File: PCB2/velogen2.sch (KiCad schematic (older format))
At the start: 34 parts, among them J1 DYN, J2 Conn_01x05_Male, J3 AUX0, J4 AUX1, J5 AUX2, J6 BAT, Q1 BSS123, Q2 DMP10H400SE, SW1 SW_SPST, U1 DCDC_mod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

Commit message: Added Schottkey diode; Clean up ERC
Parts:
- added D6, D7: B5819WS, Diode_SMD:D_SOD-323, symbol Device:D_Schottky
- C1, C2, C3, C4: symbol Device:C -> velogen2-rescue:C-Device
- D1, D2, D3, D4: symbol Device:D_Schottky -> velogen2-rescue:D_Schottky-Device
- D5: symbol Device:D_Zener -> velogen2-rescue:D_Zener-Device
- J1, J6: symbol Connector:Conn_01x02_Male -> velogen2-rescue:Conn_01x02_Male-Connector
- J2: symbol Connector:Conn_01x05_Male -> velogen2-rescue:Conn_01x05_Male-Connector
- J3, J4, J5: symbol Connector:Conn_01x03_Male -> velogen2-rescue:Conn_01x03_Male-Connector
- Q1: symbol Transistor_FET:BSS123 -> velogen2-rescue:BSS123-Transistor_FET
- Q2: symbol Device:Q_PMOS_GDS -> velogen2-rescue:Q_PMOS_GDS-Device
- R1, R2, R3, R4, R5, R6, R7: symbol Device:R -> velogen2-rescue:R-Device
- SW1: symbol Switch:SW_SPST -> velogen2-rescue:SW_SPST-Switch
- TP1, TP2, TP3, TP4: symbol Connector:TestPoint -> velogen2-rescue:TestPoint-Connector
- U1: symbol myStuff:DCDC_mod -> velogen2-rescue:DCDC_mod-myStuff
- U2: symbol RF_Module:ESP32-WROOM-32 -> velogen2-rescue:ESP32-WROOM-32-RF_Module
- U3: symbol Analog_ADC:INA219BxD -> velogen2-rescue:INA219BxD-Analog_ADC
- U4: symbol myStuff:DISP_I2C_EBAY -> velogen2-rescue:DISP_I2C_EBAY-myStuff
- U5: symbol myStuff:POGO_PROG -> velogen2-rescue:POGO_PROG-myStuff
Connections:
- net +3V3: now also D6.1 (K)
- net GND: now also D7.2 (A)
- net speedPulse: now also D6.2 (A), D7.1 (K)
- no-connect marks 0 -> 13

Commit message: clean up schematic symbols
  * re-associate standard symbols with the standard library (needs to be
    installed)
  * remove `myStuff` library. Symbols from there are now in rescue.lib
  * make the 3V3 enable switch a jumper poking out trough the case
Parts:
- removed Q1: BSS123, Package_TO_SOT_SMD:SOT-23, symbol velogen2-rescue:BSS123-Transistor_FET
- added Q1: BSS138, Package_TO_SOT_SMD:SOT-23, symbol Transistor_FET:BSS138
- C1, C2, C3, C4: symbol velogen2-rescue:C-Device -> Device:C
- D1, D2, D3, D4: symbol velogen2-rescue:D_Schottky-Device -> Device:D_Schottky
- D5: symbol velogen2-rescue:D_Zener-Device -> Device:D_Zener
- J1, J6: symbol velogen2-rescue:Conn_01x02_Male-Connector -> Connector:Conn_01x02_Male
- J2: symbol velogen2-rescue:Conn_01x05_Male-Connector -> Connector:Conn_01x05_Male
- J3, J4, J5: symbol velogen2-rescue:Conn_01x03_Male-Connector -> Connector:Conn_01x03_Male
- Q2: symbol velogen2-rescue:Q_PMOS_GDS-Device -> Device:Q_PMOS_GDS
- R1, R2, R3, R4, R5, R6, R7: symbol velogen2-rescue:R-Device -> Device:R
- SW1: footprint Connector_JST:JST_EH_B2B-EH-A_1x02_P2.50mm_Vertical -> Connector_PinHeader_2.54mm:PinHeader_1x02_P2.54mm_Horizontal; symbol velogen2-rescue:SW_SPST-Switch -> Switch:SW_SPST
- TP1, TP2, TP3, TP4: symbol velogen2-rescue:TestPoint-Connector -> Connector:TestPoint
- U2: symbol velogen2-rescue:ESP32-WROOM-32-RF_Module -> RF_Module:ESP32-WROOM-32
- U3: symbol velogen2-rescue:INA219BxD-Analog_ADC -> Analog_ADC:INA219BxD

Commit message: sch: fix some component names
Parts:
- removed Q1: BSS138, Package_TO_SOT_SMD:SOT-23, symbol Transistor_FET:BSS138
- added Q1: BSS123, Package_TO_SOT_SMD:SOT-23, symbol Transistor_FET:BSS123
- D1, D2, D3, D4: value SS32 -> SS310
- SW1: value SW_SPST -> JMP
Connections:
- wire segments 87 -> 88
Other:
- moved on the sheet: D6, D7
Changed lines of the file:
@@
 encoding utf-8
 Sheet 1 1
-Title ""
-Date ""
-Rev ""
+Title "Velogen"
+Date "2020-09-22"
+Rev "-"
 Comp ""
 Comment1 ""
@@
 P 1550 1400
 F 0 "D1" V 1504 1480 50  0000 L CNN
-F 1 "SS32" V 1595 1480 50  0000 L CNN
+F 1 "SS310" V 1595 1480 50  0000 L CNN
 F 2 "Diode_SMD:D_SMC" H 1550 1400 50  0001 C CNN
 F 3 "~" H 1550 1400 50  0001 C CNN
@@
 P 2300 1400
 F 0 "D3" V 2254 1480 50  0000 L CNN
-F 1 "SS32" V 2345 1480 50  0000 L CNN
+F 1 "SS310" V 2345 1480 50  0000 L CNN
 F 2 "Diode_SMD:D_SMC" H 2300 1400 50  0001 C CNN
 F 3 "~" H 2300 1400 50  0001 C CNN
@@
 P 1550 1800
 F 0 "D2" V 1504 1880 50  0000 L CNN
-F 1 "SS32" V 1595 1880 50  0000 L CNN
+F 1 "SS310" V 1595 1880 50  0000 L CNN
 F 2 "Diode_SMD:D_SMC" H 1550 1800 50  0001 C CNN
 F 3 "~" H 1550 1800 50  0001 C CNN
@@
 P 2300 1800
 F 0 "D4" V 2254 1880 50  0000 L CNN
-F 1 "SS32" V 2345 1880 50  0000 L CNN
+F 1 "SS310" V 2345 1880 50  0000 L CNN
 F 2 "Diode_SMD:D_SMC" H 2300 1800 50  0001 C CNN
 F 3 "~" H 2300 1800 50  0001 C CNN
@@
 P 1550 5150
 F 0 "SW1" V 1504 5248 50  0000 L CNN
-F 1 "SW_SPST" V 1595 5248 50  0000 L CNN
+F 1 "JMP" V 1595 5248 50  0000 L CNN
 F 2 "Connector_PinHeader_2.54mm:PinHeader_1x02_P2.54mm_Horizontal" H 1550 5150 50  0001 C CNN
 F 3 "~" H 1550 5150 50  0001 C CNN
@@
 Wire Wire Line
 	2750 1750 2750 1600
-Text Label 2750 2550 1    50   ~ 0
+Text Label 3200 3000 2    50   ~ 0
 speedPulse
 Text Label 6750 3750 2    50   ~ 0
@@
 L Device:D_Schottky D6
 U 1 1 5F65588B
-P 2850 3050
-F 0 "D6" H 2850 3267 50  0000 C CNN
-F 1 "B5819WS" H 2850 3176 50  0000 C CNN
-F 2 "Diode_SMD:D_SOD-323" H 2850 3050 50  0001 C CNN
-F 3 "https://www.mccsemi.com/pdf/Products/B5817WS-B5819WS(SOD-323).PDF" H 2850 3050 50  0001 C CNN
-	1    2850 3050
+P 2450 2800
+F 0 "D6" H 2450 3017 50  0000 C CNN
+F 1 "B5819WS" H 2450 2926 50  0000 C CNN
+F 2 "Diode_SMD:D_SOD-323" H 2450 2800 50  0001 C CNN
+F 3 "https://www.mccsemi.com/pdf/Products/B5817WS-B5819WS(SOD-323).PDF" H 2450 2800 50  0001 C CNN
+	1    2450 2800
 	0    1    1    0
 $EndComp
@@
 L Device:D_Schottky D7
 U 1 1 5F657E57
-P 2850 3650
-F 0 "D7" H 2850 3867 50  0000 C CNN
-F 1 "B5819WS" H 2850 3776 50  0000 C CNN
-F 2 "Diode_SMD:D_SOD-323" H 2850 3650 50  0001 C CNN
-F 3 "https://www.mccsemi.com/pdf/Products/B5817WS-B5819WS(SOD-323).PDF" H 2850 3650 50  0001 C CNN
-	1    2850 3650
-	0    1    1    0
-$EndComp
-Wire Wire Line
-	2850 3200 2850 3350
-Wire Wire Line
-	2850 3350 2750 3350
-Connection ~ 2850 3350
-Wire Wire Line
-	2850 3350 2850 3500
-Wire Wire Line
-	2750 2050 2750 3350
+P 2450 3200
+F 0 "D7" H 2450 3417 50  0000 C CNN
+F 1 "B5819WS" H 2450 3326 50  0000 C CNN
+F 2 "Diode_SMD:D_SOD-323" H 2450 3200 50  0001 C CNN
+F 3 "https://www.mccsemi.com/pdf/Products/B5817WS-B5819WS(SOD-323).PDF" H 2450 3200 50  0001 C CNN
+	1    2450 3200
+	0    1    1    0
+$EndComp
+Wire Wire Line
+	2450 2950 2450 3000
+Connection ~ 2450 3000
+Wire Wire Line
+	2450 3000 2450 3050
+Wire Wire Line
+	2750 2050 2750 3000
 $Comp
 L power:+3V3 #PWR04
 U 1 1 5F688C96
-P 2850 2900
-F 0 "#PWR04" H 2850 2750 50  0001 C CNN
-F 1 "+3V3" H 2865 3073 50  0000 C CNN
-F 2 "" H 2850 2900 50  0001 C CNN
-F 3 "" H 2850 2900 50  0001 C CNN
-	1    2850 2900
+P 2450 2650
+F 0 "#PWR04" H 2450 2500 50  0001 C CNN
+F 1 "+3V3" H 2465 2823 50  0000 C CNN
+F 2 "" H 2450 2650 50  0001 C CNN
+F 3 "" H 2450 2650 50  0001 C CNN
+	1    2450 2650
 	1    0    0    -1
 $EndComp
@@
 L power:GND #PWR05
 U 1 1 5F6962B6
-P 2850 3800
-F 0 "#PWR05" H 2850 3550 50  0001 C CNN
-F 1 "GND" H 2855 3627 50  0000 C CNN
-F 2 "" H 2850 3800 50  0001 C CNN
-F 3 "" H 2850 3800 50  0001 C CNN
-	1    2850 3800
+P 2450 3350
+F 0 "#PWR05" H 2450 3100 50  0001 C CNN
+F 1 "GND" H 2455 3177 50  0000 C CNN
+F 2 "" H 2450 3350 50  0001 C CNN
+F 3 "" H 2450 3350 50  0001 C CNN
+	1    2450 3350
 	1    0    0    -1
 $EndComp
@@
 NoConn ~ 5050 5250
 $Comp
-L Transistor_FET:BSS138 Q1
-U 1 1 5F65DFE4
+L Transistor_FET:BSS123 Q1
+U 1 1 5F6AB46B
 P 3350 2200
 F 0 "Q1" H 3555 2246 50  0000 L CNN
-F 1 "BSS138" H 3555 2155 50  0000 L CNN
+F 1 "BSS123" H 3555 2155 50  0000 L CNN
 F 2 "Package_TO_SOT_SMD:SOT-23" H 3550 2125 50  0001 L CIN
-F 3 "https://www.onsemi.com/pub/Collateral/BSS138-D.PDF" H 3350 2200 50  0001 L CNN
+F 3 "http://www.diodes.com/assets/Datasheets/ds30366.pdf" H 3350 2200 50  0001 L CNN
 	1    3350 2200
 	-1   0    0    -1
 $EndComp
+Wire Wire Line
+	2450 3000 2750 3000
+Connection ~ 2750 3000
+Wire Wire Line
+	2750 3000 3200 3000
 $EndSCHEMATC

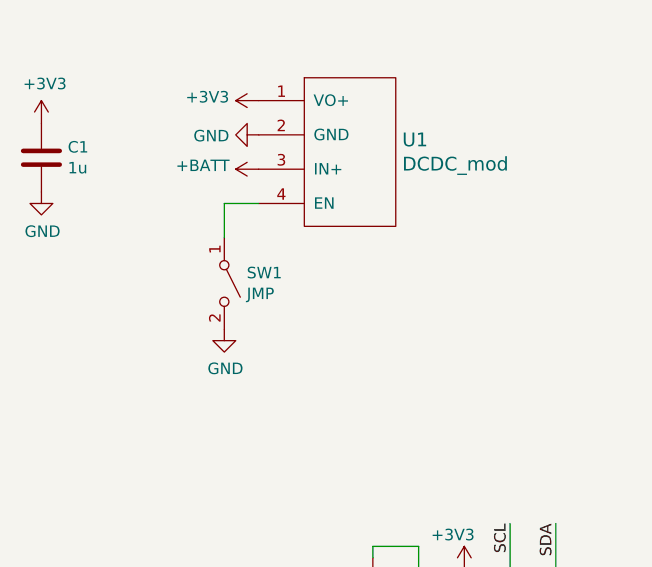
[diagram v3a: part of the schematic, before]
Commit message: put propper package (SMA) for diodes
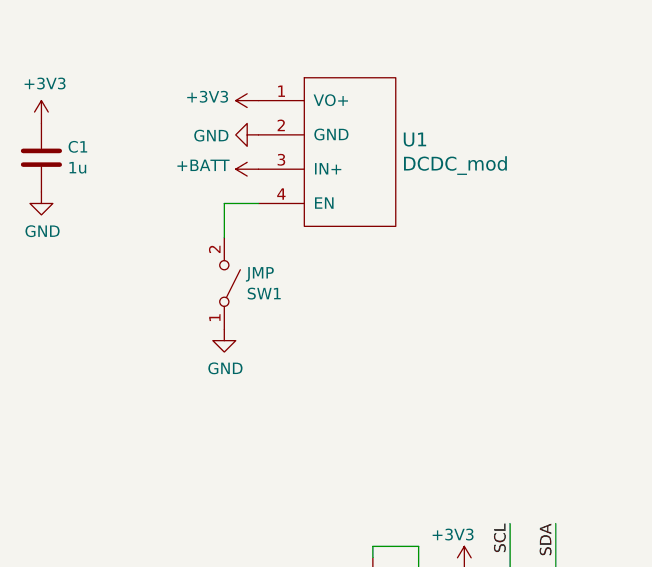
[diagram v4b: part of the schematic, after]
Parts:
- D1, D2, D3, D4: footprint Diode_SMD:D_SMC -> Diode_SMD:D_SMA
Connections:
- net GND: now also SW1.1 (A); no longer SW1.2 (B)
- net at U1.4 (EN): now also SW1.2 (B); no longer SW1.1 (A)
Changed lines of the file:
@@
 F 0 "D1" V 1504 1480 50  0000 L CNN
 F 1 "SS310" V 1595 1480 50  0000 L CNN
-F 2 "Diode_SMD:D_SMC" H 1550 1400 50  0001 C CNN
+F 2 "Diode_SMD:D_SMA" H 1550 1400 50  0001 C CNN
 F 3 "~" H 1550 1400 50  0001 C CNN
 	1    1550 1400
@@
 F 0 "D3" V 2254 1480 50  0000 L CNN
 F 1 "SS310" V 2345 1480 50  0000 L CNN
-F 2 "Diode_SMD:D_SMC" H 2300 1400 50  0001 C CNN
+F 2 "Diode_SMD:D_SMA" H 2300 1400 50  0001 C CNN
 F 3 "~" H 2300 1400 50  0001 C CNN
 	1    2300 1400
@@
 F 0 "D2" V 1504 1880 50  0000 L CNN
 F 1 "SS310" V 1595 1880 50  0000 L CNN
-F 2 "Diode_SMD:D_SMC" H 1550 1800 50  0001 C CNN
+F 2 "Diode_SMD:D_SMA" H 1550 1800 50  0001 C CNN
 F 3 "~" H 1550 1800 50  0001 C CNN
 	1    1550 1800
@@
 F 0 "D4" V 2254 1880 50  0000 L CNN
 F 1 "SS310" V 2345 1880 50  0000 L CNN
-F 2 "Diode_SMD:D_SMC" H 2300 1800 50  0001 C CNN
+F 2 "Diode_SMD:D_SMA" H 2300 1800 50  0001 C CNN
 F 3 "~" H 2300 1800 50  0001 C CNN
 	1    2300 1800
@@
 F 3 "~" H 1550 5150 50  0001 C CNN
 	1    1550 5150
-	0    1    1    0
-$EndComp
-Wire Wire Line
+	0    1    -1   0
+$EndComp
+Wire Wire Line

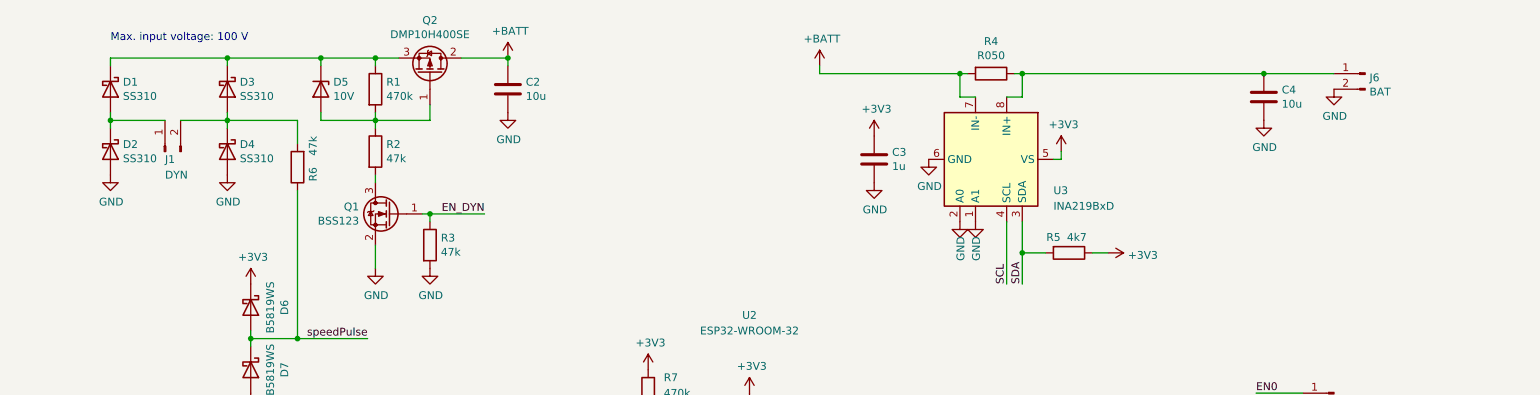
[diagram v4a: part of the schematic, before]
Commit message: did some routing of the power rails
  * kinda stuck on the 3V3, might need to re-consider placement
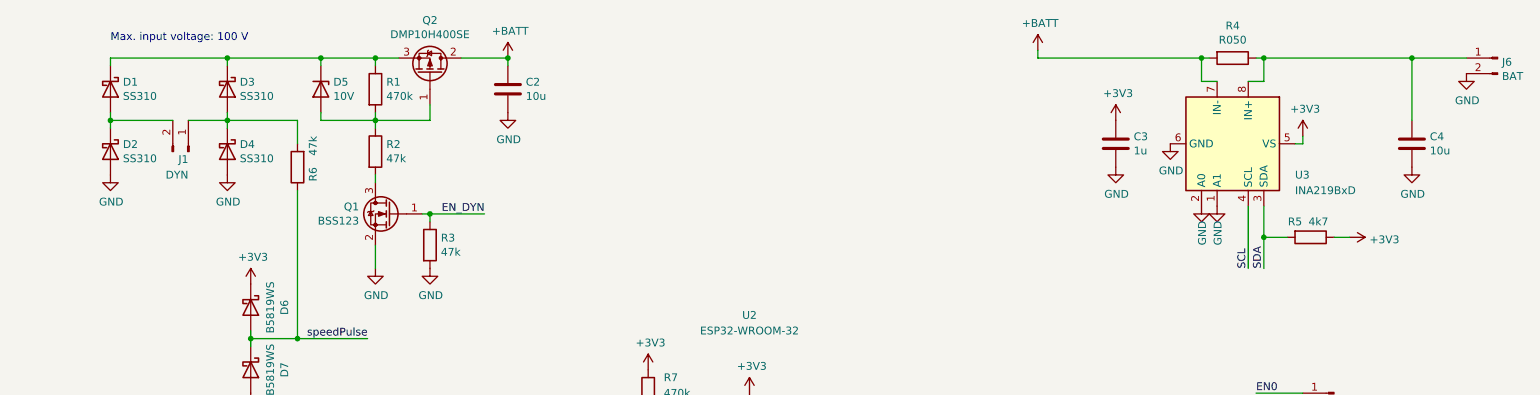
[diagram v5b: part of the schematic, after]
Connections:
- net at D1.2 (A), D2.1 (K): now also J1.2 (Pin_2); no longer J1.1 (Pin_1)
- net at D3.2 (A), D4.1 (K), R6.2: now also J1.1 (Pin_1); no longer J1.2 (Pin_2)
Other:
- moved on the sheet: C3, C4, J1, J6, R4, R5, U3

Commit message: das Schwein ist bestellt!
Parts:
- removed J2: Conn_01x05_Male, Connector_JST:JST_XH_S5B-XH-A-1_1x05_P2.50mm_Horizontal, symbol Connector:Conn_01x05_Male
- removed SW1: JMP, Connector_PinHeader_2.54mm:PinHeader_1x02_P2.54mm_Horizontal, symbol Switch:SW_SPST
- removed U1: DCDC_mod, myStuff:ebay_dcdc, symbol velogen2-rescue:DCDC_mod-myStuff
- added C5: 10u, Capacitor_SMD:C_0603_1608Metric, symbol Device:C
- added C6: 1u, Capacitor_SMD:C_0805_2012Metric, symbol Device:C
- added L1: DO1608C-223MLB, myStuff:DO1608, symbol Device:L
- added R8: 13k3, Resistor_SMD:R_0805_2012Metric, symbol Device:R
- added R9: 41k2, Resistor_SMD:R_0805_2012Metric, symbol Device:R
- added U1: TPS560200, Package_TO_SOT_SMD:SOT-23-5, symbol Regulator_Switching:TPS560200
- C1: value 1u -> 10u; footprint Capacitor_SMD:C_0805_2012Metric -> Capacitor_SMD:C_0603_1608Metric
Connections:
- wire segments 89 -> 92
- no-connect marks 13 -> 20
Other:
- moved on the sheet: C1, D6, D7, R5, R6, TP1, TP2, TP3, TP4

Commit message: cad: tune the PCB shell, add oled spacer
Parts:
- R8: value 13k3 -> 15k
- R9: value 41k2 -> 47k
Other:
- note added: "IO12 should be 0V at boot to get 3V3 flash voltage\nworkaround:\nespefuse.py set_flash_voltage 3.3V"
- note added: "should be 0603, 10uF"
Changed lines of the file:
@@
 P 1750 5250
 F 0 "R8" H 1650 5250 50  0000 R CNN
-F 1 "13k3" H 1650 5350 50  0000 R CNN
+F 1 "15k" H 1650 5350 50  0000 R CNN
 F 2 "Resistor_SMD:R_0805_2012Metric" V 1680 5250 50  0001 C CNN
 F 3 "~" H 1750 5250 50  0001 C CNN
@@
 P 2000 5050
 F 0 "R9" V 1900 4950 50  0000 R CNN
-F 1 "41k2" V 1800 4950 50  0000 R CNN
+F 1 "47k" V 1800 4950 50  0000 R CNN
 F 2 "Resistor_SMD:R_0805_2012Metric" V 1930 5050 50  0001 C CNN
 F 3 "~" H 2000 5050 50  0001 C CNN
@@
 	1    0    0    -1
 $EndComp
+Text Notes 7000 6850 0    50   ~ 0
+IO12 should be 0V at boot to get 3V3 flash voltage\nworkaround:\nespefuse.py set_flash_voltage 3.3V
+Text Notes 6850 2900 0    50   ~ 0
+should be 0603, 10uF
+Text Notes 6950 1800 0    50   ~ 0
+should be 0603, 10uF
 $EndSCHEMATC

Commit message: work on OLED gui and simulation
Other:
- note added: "5 W, 10 V Zener or TVS is\nmandatorry on +Batt\nin case of battery has\nbad connection"
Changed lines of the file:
@@
 Text Notes 6950 1800 0    50   ~ 0
 should be 0603, 10uF
+Text Notes 4500 1500 0    50   ~ 0
+5 W, 10 V Zener or TVS is\nmandatorry on +Batt\nin case of battery has\nbad connection
 $EndSCHEMATC
